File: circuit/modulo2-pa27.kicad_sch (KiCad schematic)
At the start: 48 parts, among them J2 CONN_01X04, J3 CONN_01X04, J4 JACK_MONO, J5 HOLE, J7 HOLE, SW1 bright, U1 OPA2134, U2 OPA2134, U3 TLE2426

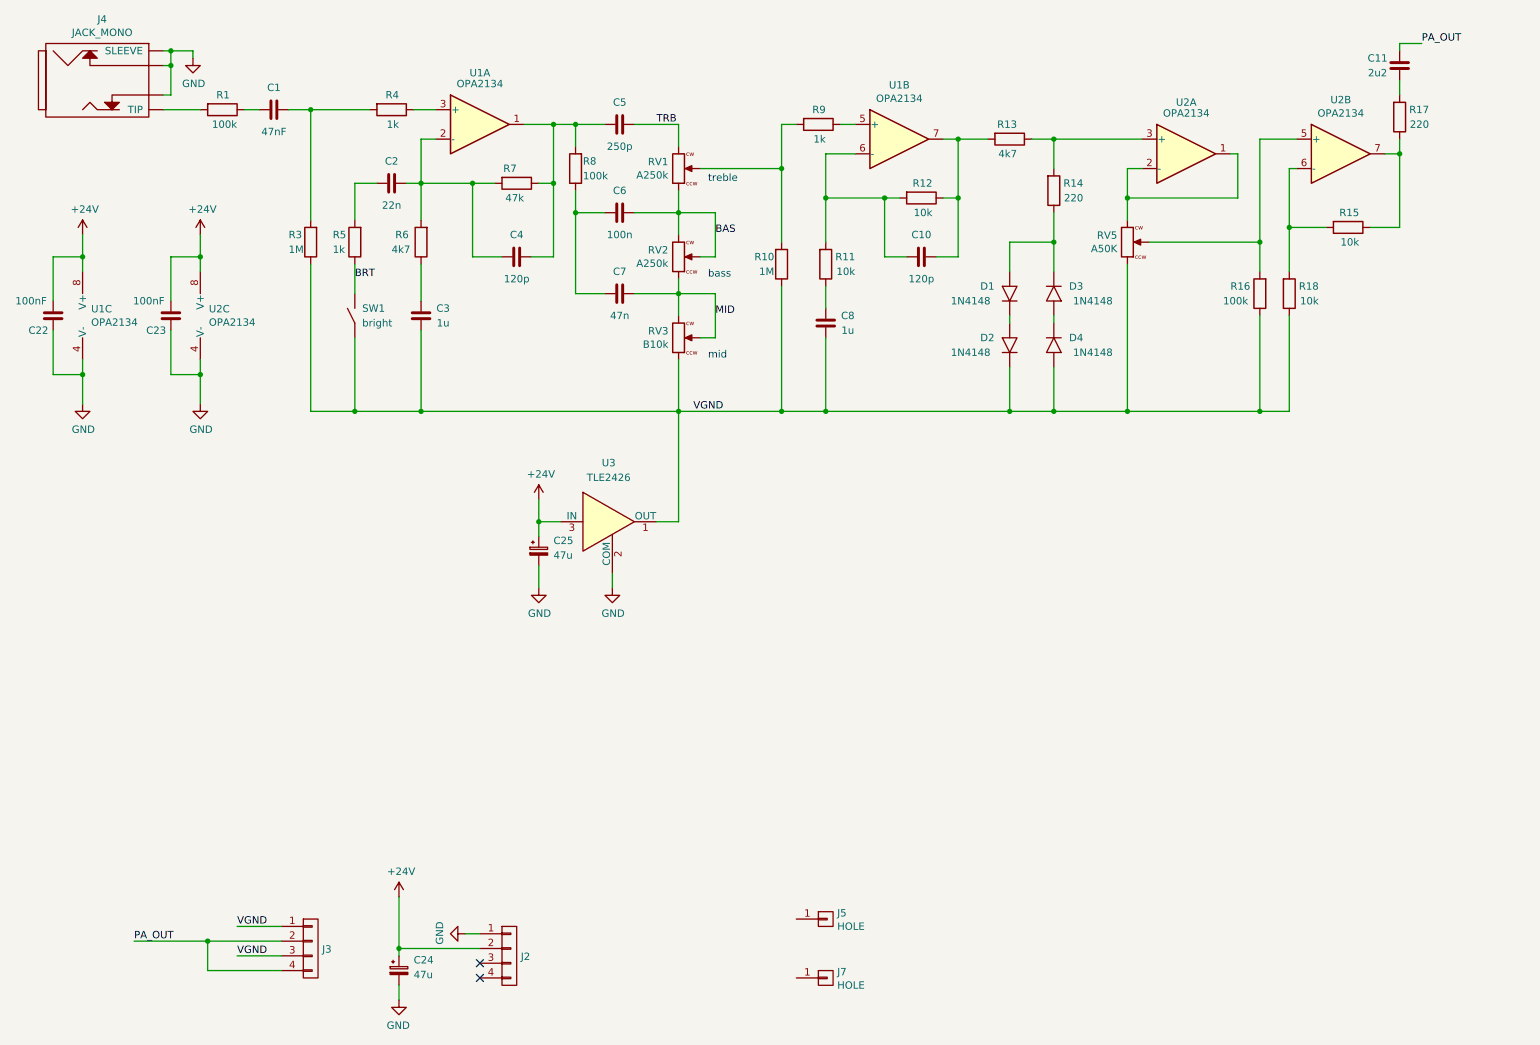
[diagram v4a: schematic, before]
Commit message: added report on createBanks.py; started PCB redesign
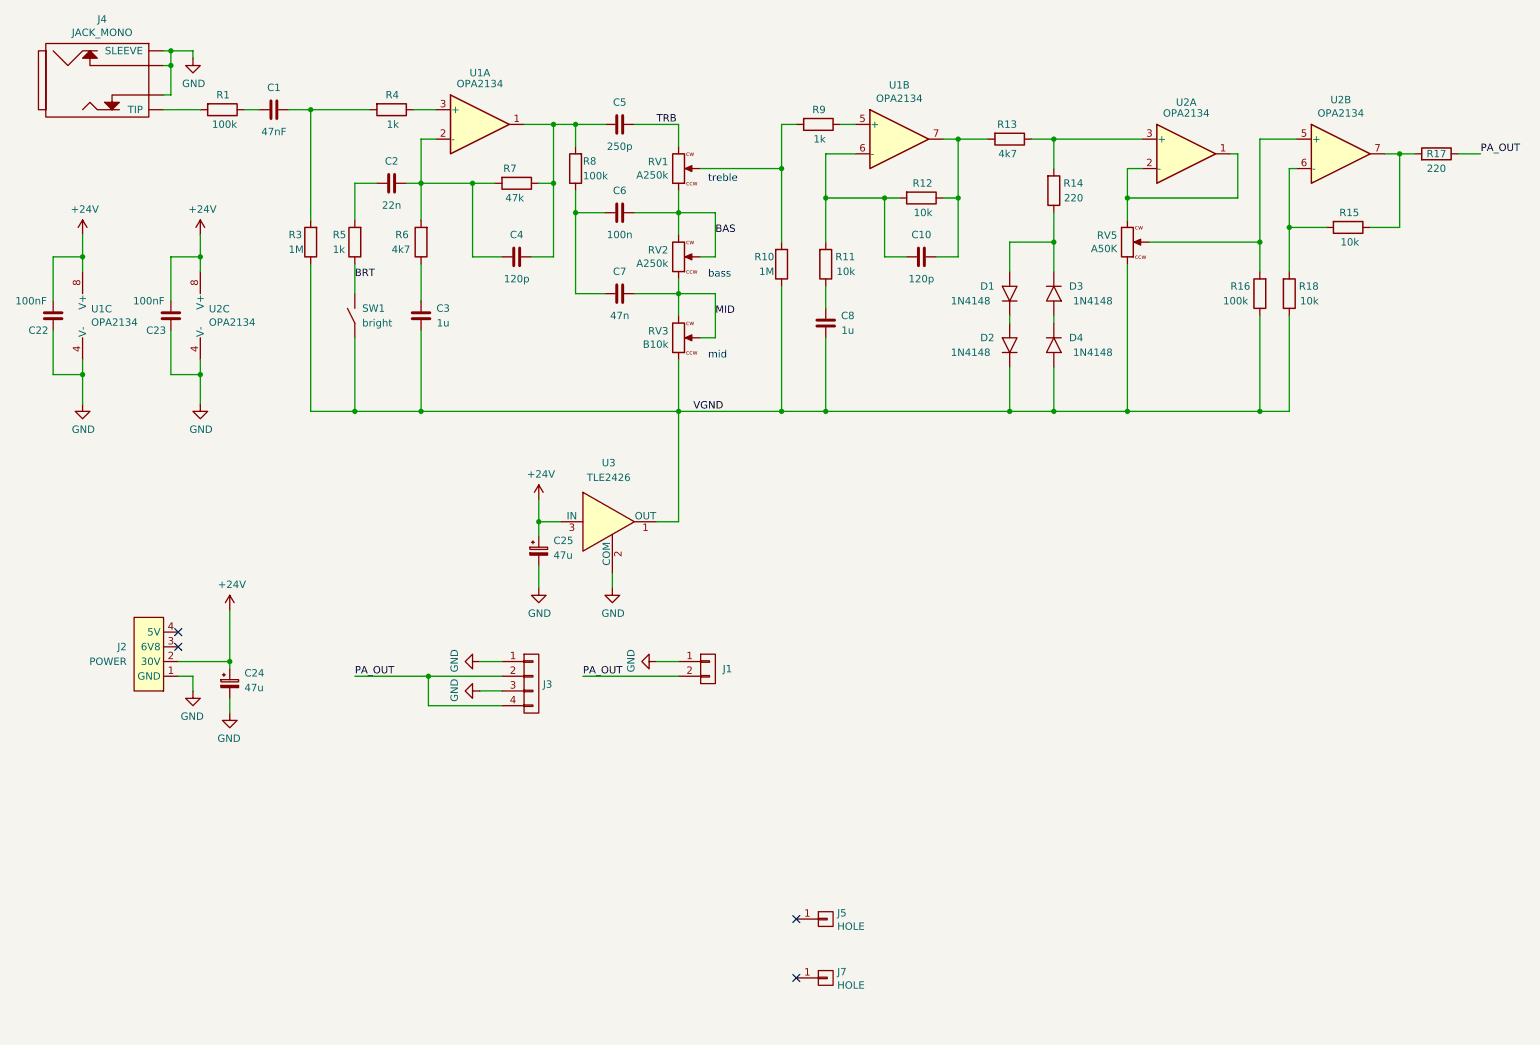
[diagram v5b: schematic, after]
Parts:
- removed C11: 2u2, myAmp:C_FILM_L7.2mm_W5.5mm_P5.00mm, symbol myAmp:C
- removed J2: CONN_01X04, myAmp:PIN_1x04, symbol myAmp:CONN_01X04
- added J1: CONN_01X02, myAmp:PIN_1x02, symbol myAmp:CONN_01X02
- added J2: POWER, myAmp:POWER, symbol myAmp:POWER
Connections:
- net +24V: now also J2.2 (30V)
- net GND: now also J3.1 (P1), J3.3, J1.1 (P1), J2.1 (GND)
- net PA_OUT: now also R17.1, J1.2 (P2)
- net VGND: no longer J3.1 (P1), J3.3
- net at R15.1, U2.7: now also R17.2; no longer R17.1
- no-connect marks 2 -> 4
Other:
- moved on the sheet: C24, J3, R17

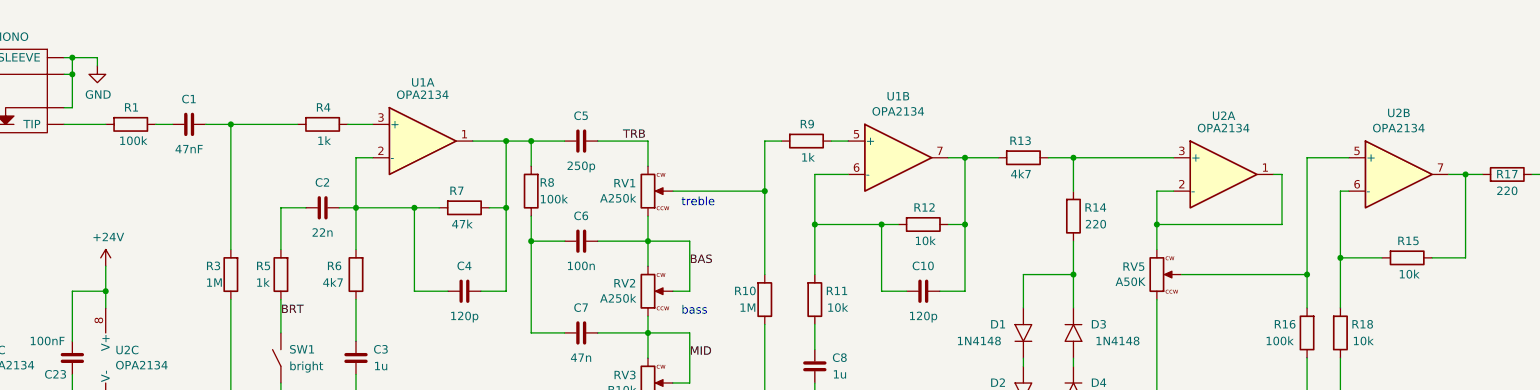
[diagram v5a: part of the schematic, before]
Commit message: further routing of FV-1
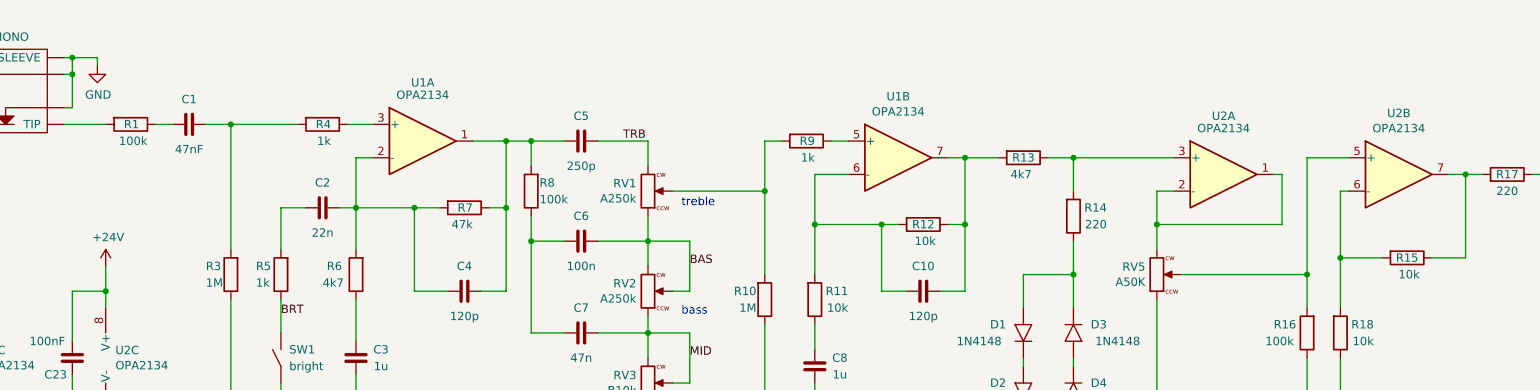
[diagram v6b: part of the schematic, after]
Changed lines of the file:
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@@
   (symbol (lib_id "myAmp:R") (at 77.47 31.75 270) (unit 1)
     (in_bom yes) (on_board yes)
-    (property "Reference" "R4" (id 0) (at 78.74 29.21 90)
+    (property "Reference" "R4" (id 0) (at 78.74 31.75 90)
       (effects (font (size 1.27 1.27)) (justify right))
     )
@@
   (symbol (lib_id "myAmp:R") (at 48.26 31.75 270) (unit 1)
     (in_bom yes) (on_board yes)
-    (property "Reference" "R1" (id 0) (at 49.53 29.21 90)
+    (property "Reference" "R1" (id 0) (at 49.53 31.75 90)
       (effects (font (size 1.27 1.27)) (justify right))
     )
@@
   (symbol (lib_id "myAmp:R") (at 168.91 46.99 270) (unit 1)
     (in_bom yes) (on_board yes)
-    (property "Reference" "R12" (id 0) (at 170.815 44.45 90)
-      (effects (font (size 1.27 1.27)) (justify right))
-    )
+    (property "Reference" "R12" (id 0) (at 168.91 46.99 90))
     (property "Value" "10k" (id 1) (at 170.815 49.53 90)
       (effects (font (size 1.27 1.27)) (justify right))
@@
   (symbol (lib_id "myAmp:R") (at 99.06 44.45 270) (unit 1)
     (in_bom yes) (on_board yes)
-    (property "Reference" "R7" (id 0) (at 99.06 41.91 90)
+    (property "Reference" "R7" (id 0) (at 100.33 44.45 90)
       (effects (font (size 1.27 1.27)) (justify right))
     )
@@
   (symbol (lib_id "myAmp:R") (at 242.57 52.07 270) (unit 1)
     (in_bom yes) (on_board yes)
-    (property "Reference" "R15" (id 0) (at 244.475 49.53 90)
-      (effects (font (size 1.27 1.27)) (justify right))
-    )
+    (property "Reference" "R15" (id 0) (at 242.57 52.07 90))
     (property "Value" "10k" (id 1) (at 244.475 54.61 90)
       (effects (font (size 1.27 1.27)) (justify right))
@@
   (symbol (lib_id "myAmp:R") (at 151.13 34.29 270) (unit 1)
     (in_bom yes) (on_board yes)
-    (property "Reference" "R9" (id 0) (at 152.4 31.75 90)
+    (property "Reference" "R9" (id 0) (at 152.4 34.29 90)
       (effects (font (size 1.27 1.27)) (justify right))
     )
@@
   (symbol (lib_id "myAmp:R") (at 184.15 36.83 270) (unit 1)
     (in_bom yes) (on_board yes)
-    (property "Reference" "R13" (id 0) (at 185.42 34.29 90)
-      (effects (font (size 1.27 1.27)) (justify right))
-    )
+    (property "Reference" "R13" (id 0) (at 184.15 36.83 90))
     (property "Value" "4k7" (id 1) (at 185.42 39.37 90)
       (effects (font (size 1.27 1.27)) (justify right))

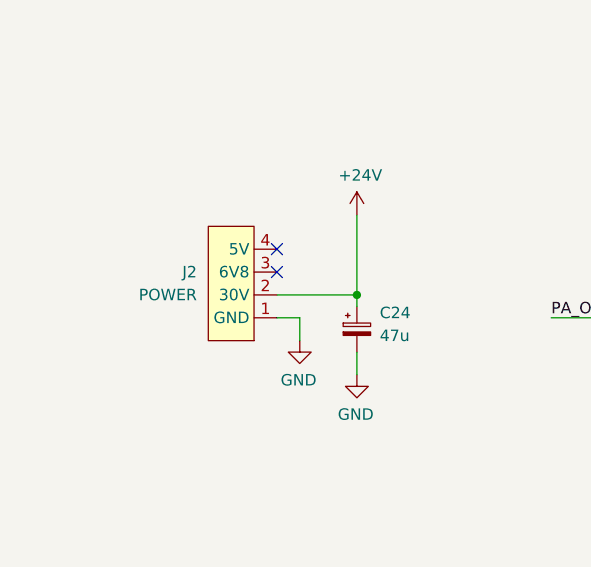
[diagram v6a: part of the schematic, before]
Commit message: no more assembler; more routing
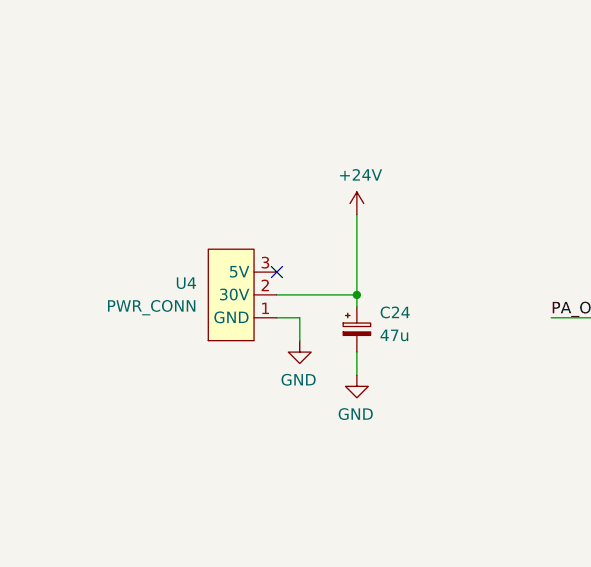
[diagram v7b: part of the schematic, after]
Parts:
- removed J2: POWER, myAmp:POWER, symbol myAmp:POWER
- added U4: PWR_CONN, myAmp:PWR_CONN, symbol myAmp:PWR_CONN
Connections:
- net +24V: now also U4.2 (30V)
- net GND: now also U4.1 (GND)
- no-connect marks 4 -> 3
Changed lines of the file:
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@@
   (no_connect (at 147.32 181.61))
   (no_connect (at 147.32 171.45))
-  (no_connect (at 40.64 121.92))
   (no_connect (at 40.64 124.46))
   (wire (pts (xy 81.28 31.75) (xy 85.09 31.75))
@@
     (pin "2")
   )
-  (symbol (lib_id "myAmp:POWER") (at 36.83 125.73 0) (mirror x) (unit 1)
+  (symbol (lib_id "myAmp:PWR_CONN") (at 36.83 127 0) (mirror x) (unit 1)
     (in_bom yes) (on_board yes) (fields_autoplaced)
-    (property "Reference" "J2" (id 0) (at 31.75 124.4599 0)
-      (effects (font (size 1.27 1.27)) (justify right))
-    )
-    (property "Value" "POWER" (id 1) (at 31.75 126.9999 0)
-      (effects (font (size 1.27 1.27)) (justify right))
-    )
-    (property "Footprint" "myAmp:POWER" (id 2) (at 39.37 125.73 0)
+    (property "Reference" "U4" (id 0) (at 31.75 125.7299 0)
+      (effects (font (size 1.27 1.27)) (justify right))
+    )
+    (property "Value" "PWR_CONN" (id 1) (at 31.75 128.2699 0)
+      (effects (font (size 1.27 1.27)) (justify right))
+    )
+    (property "Footprint" "myAmp:PWR_CONN" (id 2) (at 39.37 125.73 0)
       (effects (font (size 1.27 1.27)) hide)
     )
@@
     (pin "2")
     (pin "3")
-    (pin "4")
   )
   (symbol (lib_id "power:GND") (at 115.57 114.3 0) (unit 1)
@@
       (reference "J1") (unit 1) (value "CONN_01X02") (footprint "myAmp:PIN_1x02")
     )
-    (path "/3be5bd27-9454-4a5f-b633-97d435ecd4be"
-      (reference "J2") (unit 1) (value "POWER") (footprint "myAmp:POWER")
-    )
     (path "/00000000-0000-0000-0000-000061b2338c"
       (reference "J3") (unit 1) (value "CONN_01X04") (footprint "myAmp:PIN_1x04")
@@
       (reference "U3") (unit 1) (value "TLE2426") (footprint "myAmp:TO-92_Inline_Wide")
     )
-  )
+    (path "/3f5b4c76-6eff-4c8c-8156-87ca92bc8661"
+      (reference "U4") (unit 1) (value "PWR_CONN") (footprint "myAmp:PWR_CONN")
+    )
+  )

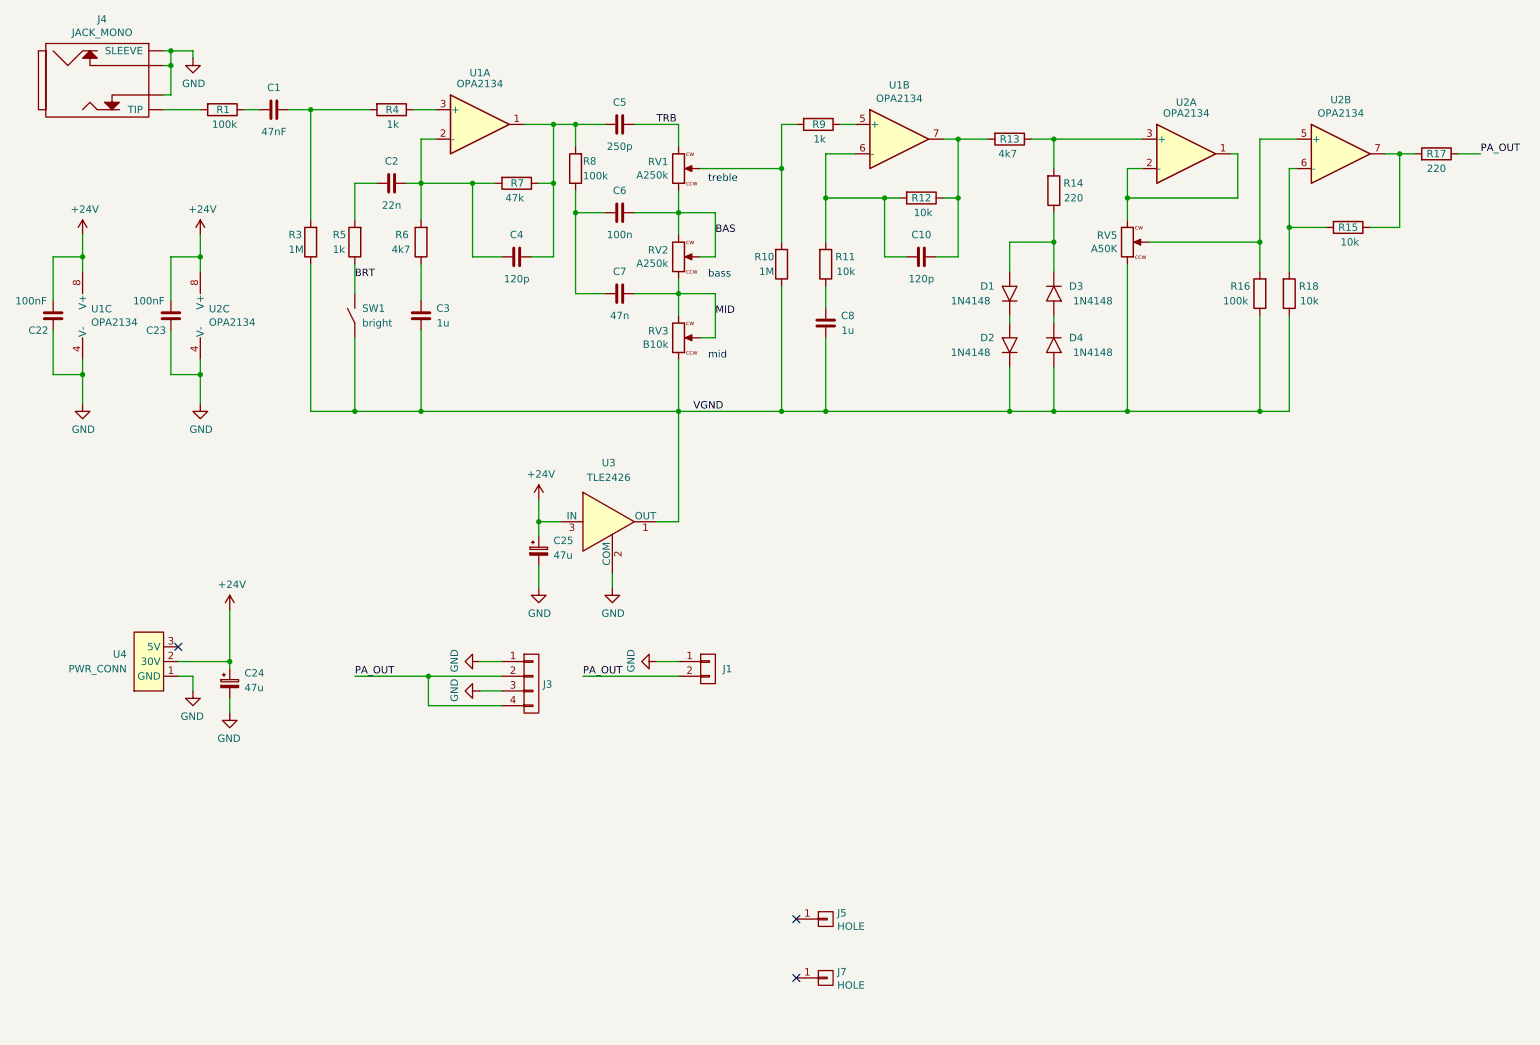
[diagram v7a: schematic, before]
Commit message: ditched the LED array board; LEDs are on the main PCB now
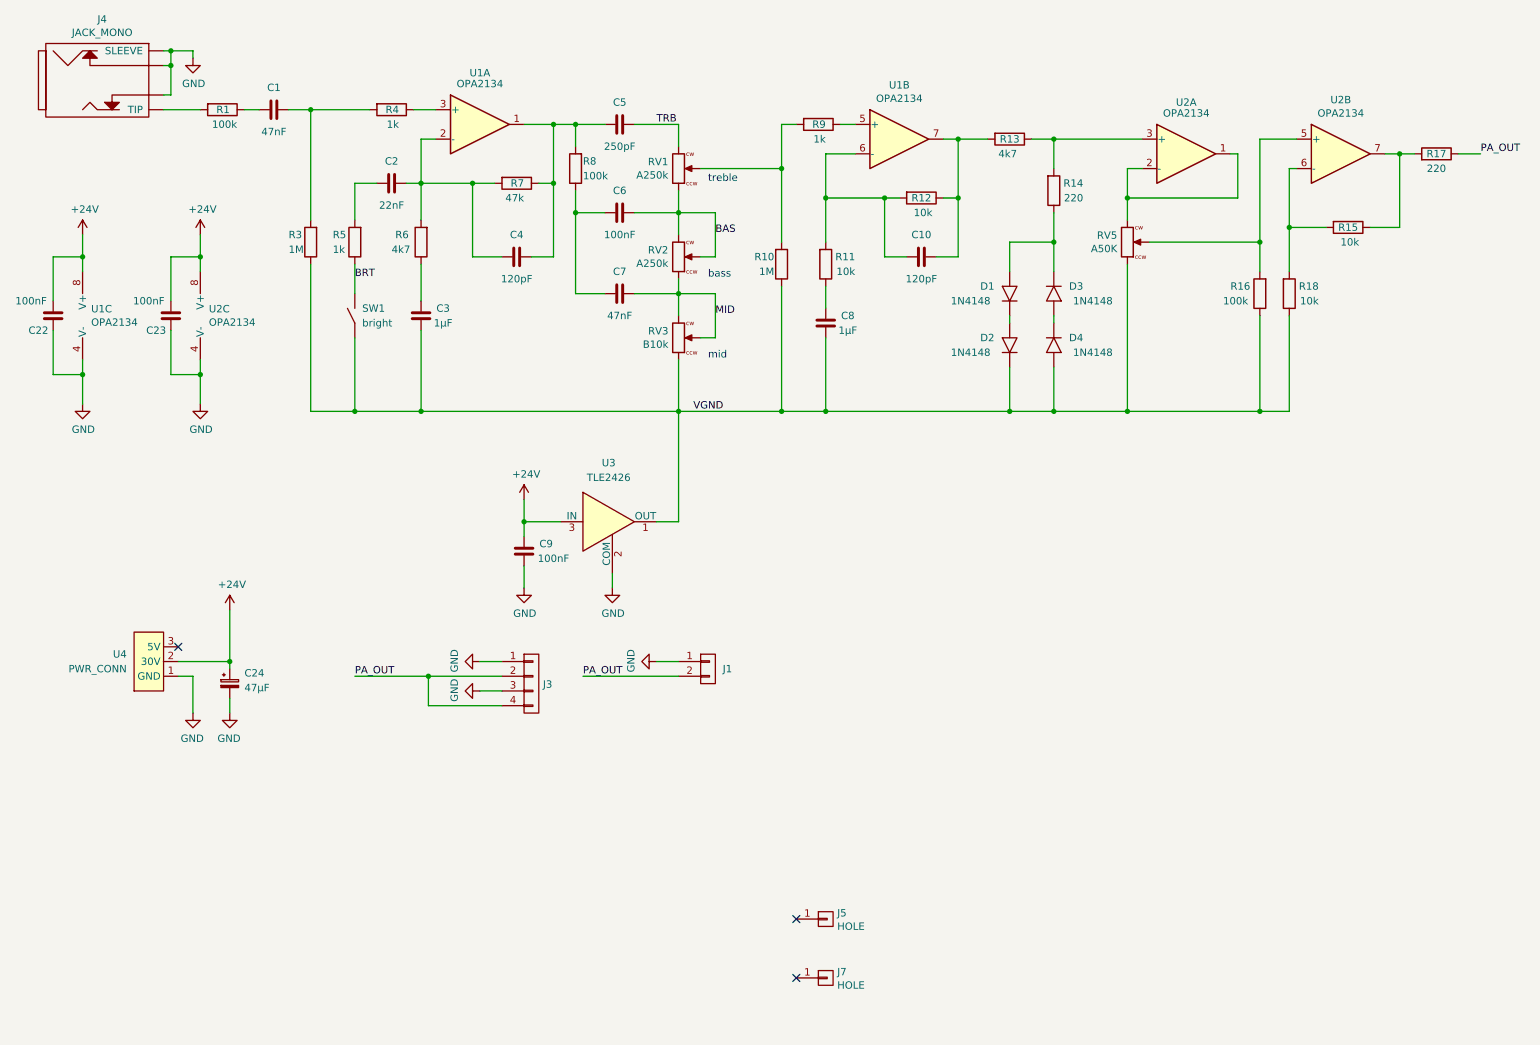
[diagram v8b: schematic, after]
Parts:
- removed C25: 47u, myAmp:CPOL_D6.3_P2.5, symbol myAmp:CPOL
- added C9: 100nF, myAmp:C_5MM_1206, symbol myAmp:C
- C10, C4: value 120p -> 120pF
- C2: value 22n -> 22nF
- C24: value 47u -> 47µF
- C3, C8: value 1u -> 1µF
- C5: value 250p -> 250pF
- C6: value 100n -> 100nF
- C7: value 47n -> 47nF
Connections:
- net +24V: now also C9.2
- net GND: now also C9.1
